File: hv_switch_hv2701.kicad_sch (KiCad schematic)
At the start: 10 parts, among them IC4 HV2701FG-G

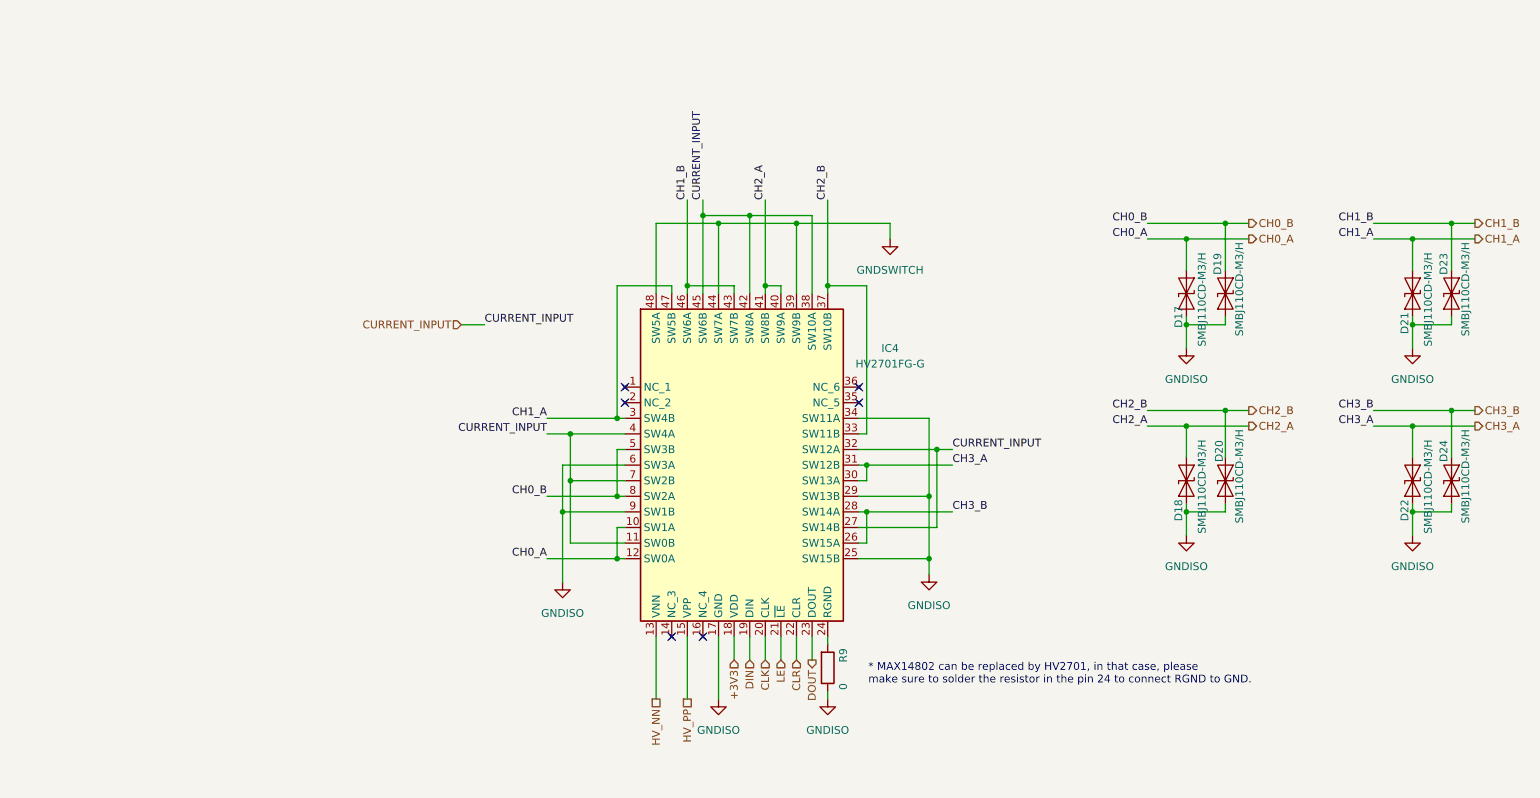
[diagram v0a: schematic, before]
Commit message: fix: replacement of ISO7641 with ISO7640
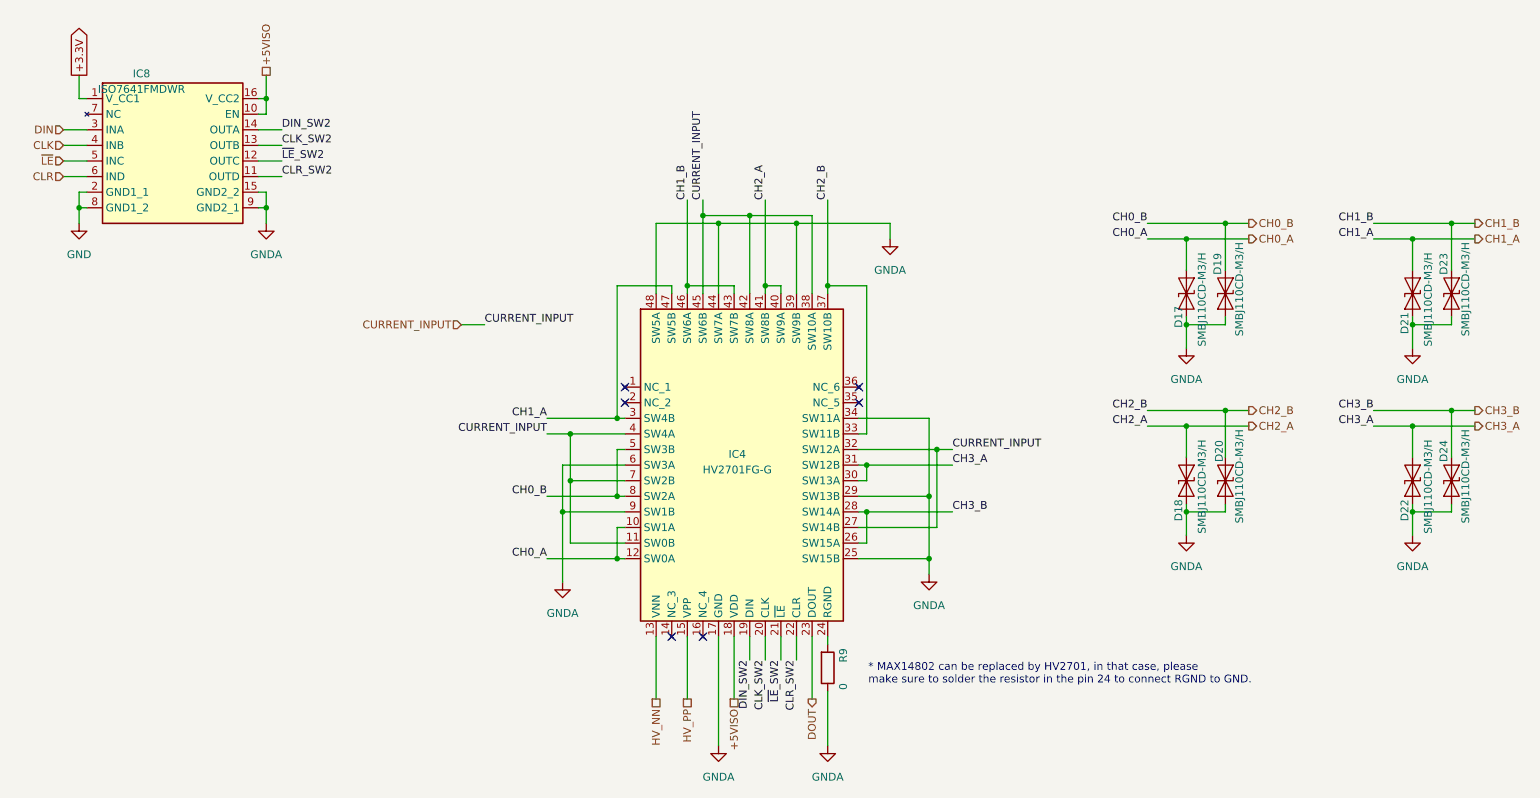
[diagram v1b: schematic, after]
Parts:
- added IC8: ISO7641FMDWR, Package_SO:SOIC-16W_7.5x10.3mm_P1.27mm, symbol Technaid:ISO7640FMDWR
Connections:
- net GNDSWITCH is gone; now on net GNDA: IC4.39 (SW9B), IC4.44 (SW7A), IC4.48 (SW5A)
- net CLK: now also IC8.4 (INB); no longer IC4.20 (CLK)
- net CLR: now also IC8.6 (IND); no longer IC4.22 (CLR)
- net DIN: now also IC8.3 (INA); no longer IC4.19 (DIN)
- net +3V3 renamed +5VISO
- net +5VISO: now also IC8.10 (EN), IC8.16 (V_CC2)
- net GNDISO renamed GNDA
- net GNDA: now also IC8.15 (GND2_2), IC8.9 (GND2_1)
- net LE renamed ~{LE}_SW2
- net ~{LE}_SW2: now also IC8.12 (OUTC)
- new net +3.3V: IC8.1 (V_CC1)
- new net CLK_SW2: IC4.20 (CLK), IC8.13 (OUTB)
- new net CLR_SW2: IC4.22 (CLR), IC8.11 (OUTD)
- new net DIN_SW2: IC4.19 (DIN), IC8.14 (OUTA)
- new net GND: IC8.2 (GND1_1), IC8.8 (GND1_2)
- new net ~{LE}: IC8.5 (INC)

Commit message: fix: update PCB with last 3dmodels and ICs (ISO7640, GNDISO)
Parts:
- removed D17, D18, D19, D20, D21, D22, D23, D24: SMBJ110CD-M3/H, Diode_SMD:D_SMA, symbol Diode:SMAJ5.0CA
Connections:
- net GNDA renamed GNDISO

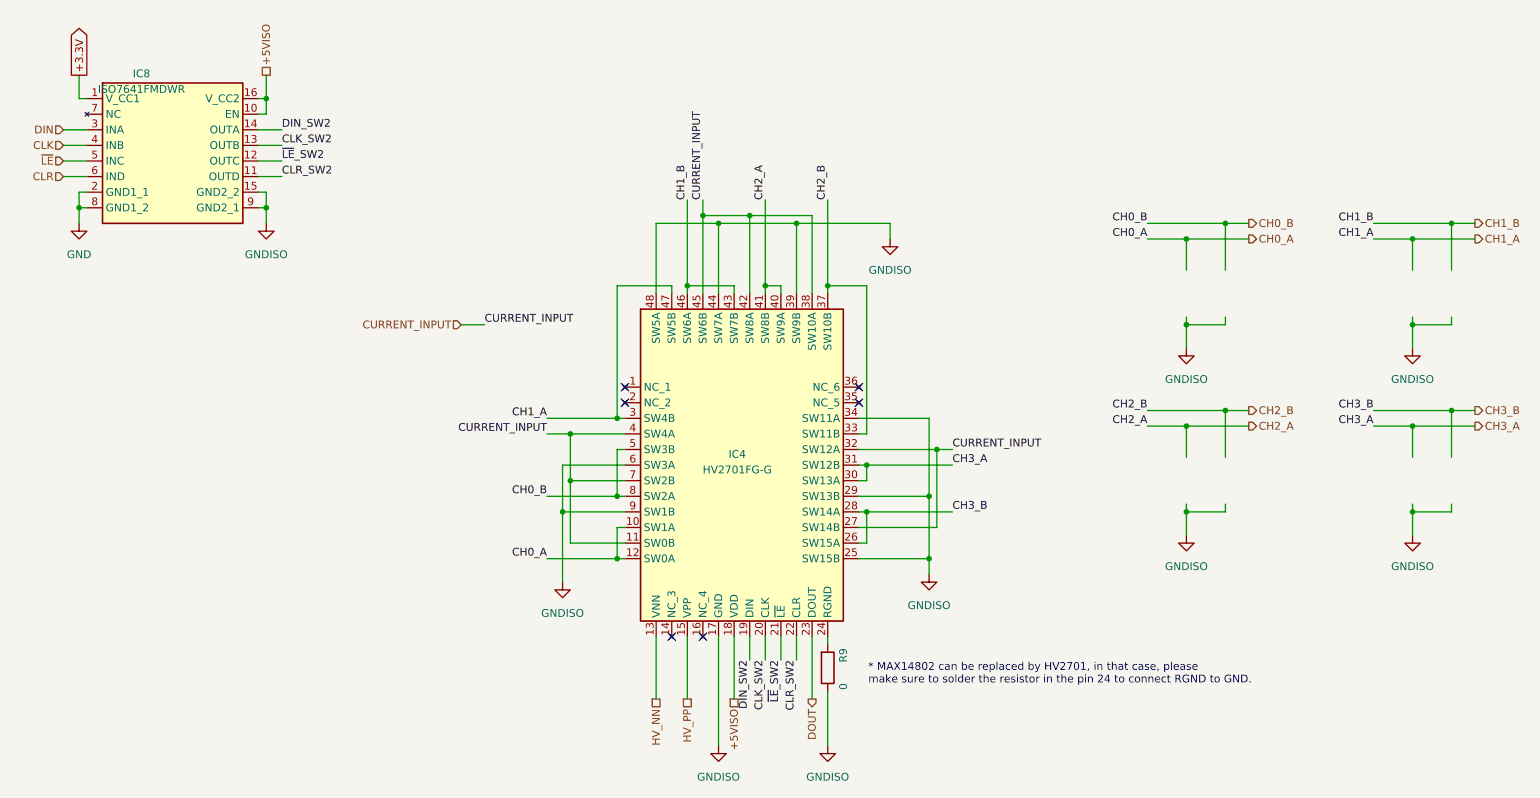
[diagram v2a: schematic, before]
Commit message: fix: adding connector to select communication between HV_Switches
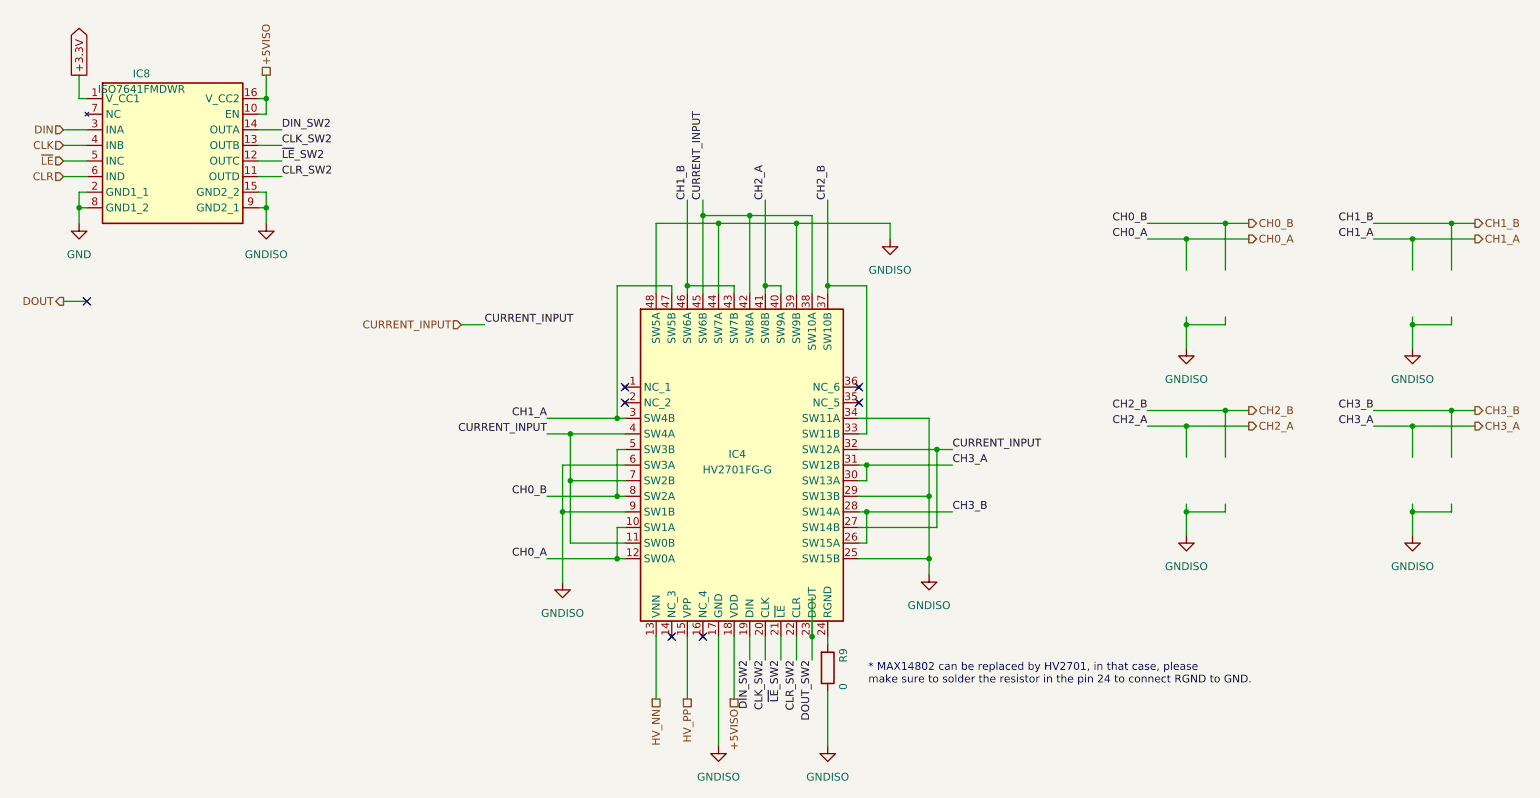
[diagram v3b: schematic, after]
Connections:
- net DOUT: no longer IC4.23 (DOUT)
- new net DOUT_SW2: IC4.23 (DOUT)
- no-connect marks 6 -> 7
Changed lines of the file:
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@@
+	)
+	(junction
+		(at 142.24 115.57)
+		(diameter 0)
+		(color 0 0 0 0)
 	)
 	(junction
@@
 		(at 149.86 77.47)
 	)
+	(no_connect
+		(at 24.13 60.96)
+	)
 	(wire
 		(pts
@@
 	(wire
 		(pts
-			(xy 142.24 115.57) (xy 142.24 125.73)
+			(xy 142.24 109.22) (xy 142.24 115.57)
 		)
 		(stroke
@@
 	(wire
 		(pts
+			(xy 20.32 60.96) (xy 24.13 60.96)
+		)
+		(stroke
+			(width 0)
+			(type default)
+		)
+	)
+	(wire
+		(pts
 			(xy 162.56 85.09) (xy 165.1 85.09)
 		)
@@
 		(pts
 			(xy 101.6 95.25) (xy 111.76 95.25)
+		)
+		(stroke
+			(width 0)
+			(type default)
+		)
+	)
+	(wire
+		(pts
+			(xy 142.24 115.57) (xy 142.24 119.38)
 		)
 		(stroke
@@
 			)
 			(justify left bottom)
+		)
+	)
+	(label "DOUT_SW2"
+		(at 142.24 119.38 270)
+		(fields_autoplaced yes)
+		(effects
+			(font
+				(size 1.27 1.27)
+			)
+			(justify right bottom)
 		)
 	)
@@
 		)
 	)
+	(hierarchical_label "DOUT"
+		(shape output)
+		(at 20.32 60.96 180)
+		(fields_autoplaced yes)
+		(effects
+			(font
+				(size 1.27 1.27)
+			)
+			(justify right)
+		)
+	)
 	(hierarchical_label "CH3_A"
 		(shape output)
@@
 		(fields_autoplaced yes)
 		(effects
-			(font
-				(size 1.27 1.27)
-			)
-			(justify right)
-		)
-	)
-	(hierarchical_label "DOUT"
-		(shape output)
-		(at 142.24 125.73 270)
-		(fields_autoplaced yes)
-		(effects

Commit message: ops: adding SP1# field and add all the info for each component
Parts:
- IC4: MFN (none) -> Microchip; MFP (none) -> HV2701FG-G; S1P# (none) -> 689-HV2701FG-G; S1PL (none) -> https://eu.mouser.com/ProductDetail/Microchip-Technology/HV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; S1PN (none) -> Mouser
- IC8: S1P# (none) -> 595-ISO7640FMDWR
- R9: S1P# (none) -> 603-RC0805FR-070RL
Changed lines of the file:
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@@
+			)
+		)
+		(property "S1P#" "595-ISO7640FMDWR"
+			(at 21.59 27.94 0)
+			(effects
+				(font
+					(size 1.27 1.27)
+				)
+				(hide yes)
 			)
 		)
@@
 			)
 		)
+		(property "S1P#" "603-RC0805FR-070RL"
+			(at 144.78 120.65 0)
+			(effects
+				(font
+					(size 1.27 1.27)
+				)
+				(hide yes)
+			)
+		)
 		(pin "2"
 		)
@@
 				(hide yes)
 			)
+		)
+		(property "MFN" "Microchip"
+			(at 114.3 62.23 0)
+			(effects
+				(font
+					(size 1.27 1.27)
+				)
+				(hide yes)
+			)
+		)
+		(property "MFP" "HV2701FG-G"
+			(at 114.3 62.23 0)
+			(effects
+				(font
+					(size 1.27 1.27)
+				)
+				(hide yes)
+			)
+		)
+		(property "S1P#" "689-HV2701FG-G"
+			(at 114.3 62.23 0)
+			(effects
+				(font
+					(size 1.27 1.27)
+				)
+				(hide yes)
+			)
+		)
+		(property "S1PL" "https://eu.mouser.com/ProductDetail/Microchip-Technology/HV2701FG-G?qs=9dFQwQorgSyz%2FfRsWmhqXg%3D%3D"
+			(at 114.3 62.23 0)
+			(effects
+				(font
+					(size 1.27 1.27)
+				)
+				(hide yes)
+			)
+		)
+		(property "S1PN" "Mouser"
+			(at 114.3 62.23 0)
+			(effects
+				(font
+					(size 1.27 1.27)
+				)
+				(hide yes)
+			)

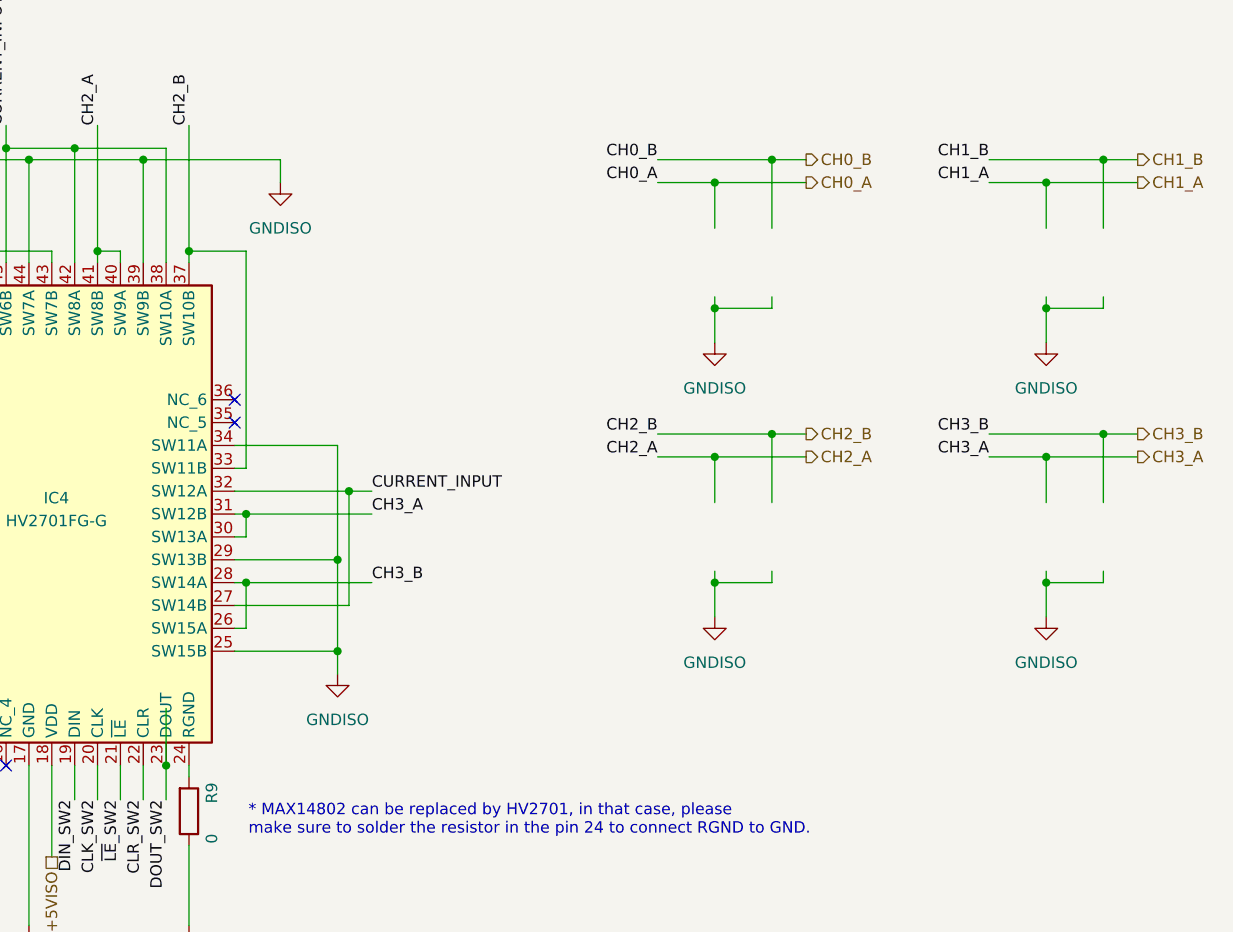
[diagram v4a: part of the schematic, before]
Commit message: fix: adding esd device in output hv2
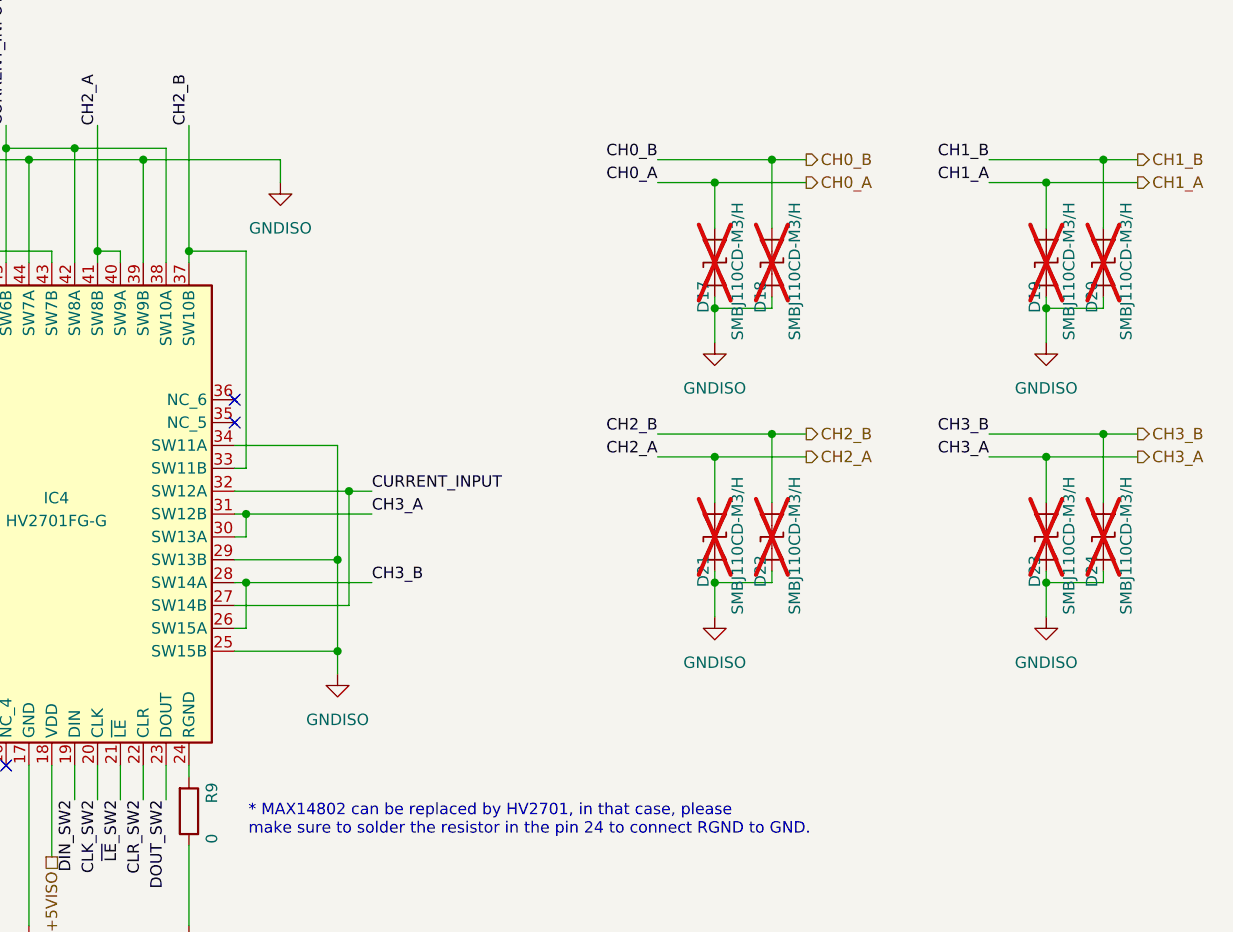
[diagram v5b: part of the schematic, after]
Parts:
- added D17, D18, D19, D20, D21, D22, D23, D24: SMBJ110CD-M3/H, Diode_SMD:D_SMA, symbol Diode:SMAJ5.0CA
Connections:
- net CH0_A: now also D17.1 (A1)
- net CH0_B: now also D18.1 (A1)
- net CH1_A: now also D19.1 (A1)
- net CH1_B: now also D20.1 (A1)
- net CH2_A: now also D21.1 (A1)
- net CH2_B: now also D22.1 (A1)
- net CH3_A: now also D23.1 (A1)
- net CH3_B: now also D24.1 (A1)
- net GNDISO: now also D17.2 (A2), D18.2 (A2), D19.2 (A2), D20.2 (A2), D21.2 (A2), D22.2 (A2), D23.2 (A2), D24.2 (A2)

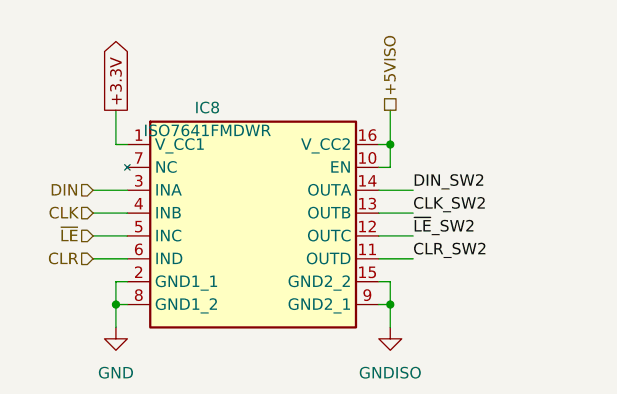
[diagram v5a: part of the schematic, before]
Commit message: fix: update names for IC components
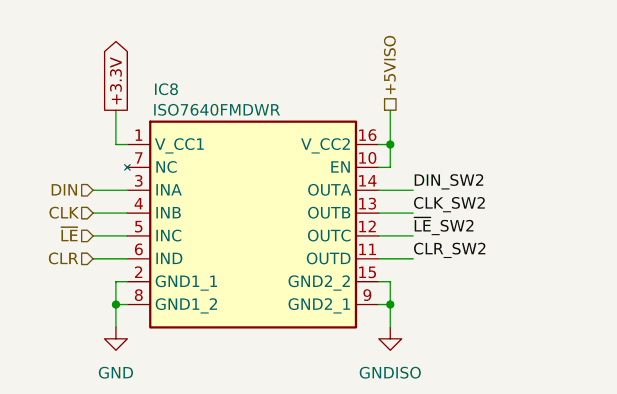
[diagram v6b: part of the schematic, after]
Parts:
- IC8: value ISO7641FMDWR -> ISO7640FMDWR
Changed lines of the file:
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@@
 		(dnp no)
 		(property "Reference" "IC8"
-			(at 33.02 23.876 0)
+			(at 28.448 21.844 0)
 			(effects
 				(font
@@
 			)
 		)
-		(property "Value" "ISO7641FMDWR"
-			(at 33.02 26.416 0)
+		(property "Value" "ISO7640FMDWR"
+			(at 34.036 24.13 0)
 			(effects
 				(font
